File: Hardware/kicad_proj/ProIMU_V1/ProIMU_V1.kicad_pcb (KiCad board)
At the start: 2 copper layers, 50 x 50 mm, 31 parts, among them J1 USB4105-GF-A, J2 502570-0893, U1 BMP280, U2 MPU-9250, U3 STM32F412CEU6, U4 AIR602, U5 POGOPIN, U6 POGOPIN, U7 POGOPIN, U8 POGOPIN, U9 POGOPIN

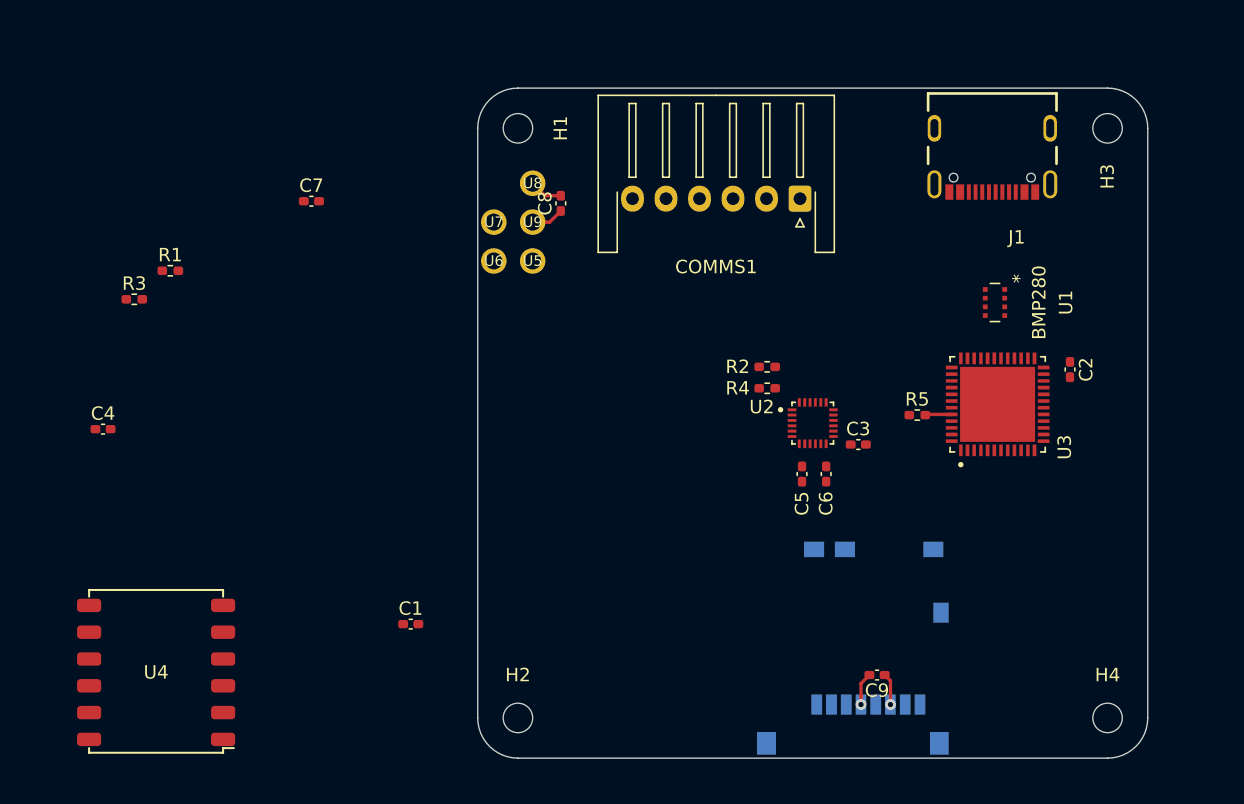
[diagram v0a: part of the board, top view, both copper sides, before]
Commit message: Update: Layout updated. Pinout needs to be revised
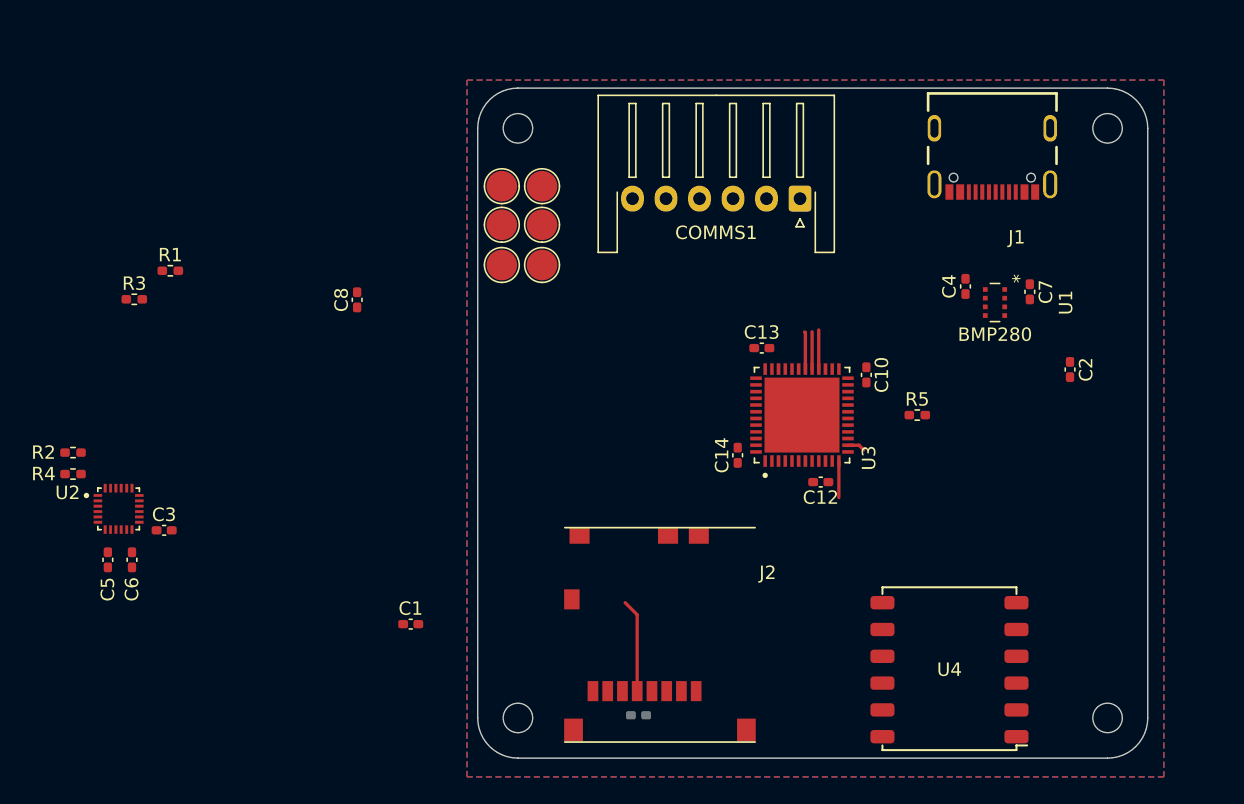
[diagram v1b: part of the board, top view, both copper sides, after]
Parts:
- added C10: 1uF, Capacitor_SMD:C_0402_1005Metric_Pad0.74x0.62mm_HandSolder, F.Cu at (155.8, 92.0)
- added C12: 1uF, Capacitor_SMD:C_0402_1005Metric_Pad0.74x0.62mm_HandSolder, F.Cu at (152.4, 100.0)
- added C13: 1uF, Capacitor_SMD:C_0402_1005Metric_Pad0.74x0.62mm_HandSolder, F.Cu at (148.0, 90.0)
- added C14: 1uF, Capacitor_SMD:C_0402_1005Metric_Pad0.74x0.62mm_HandSolder, F.Cu at (146.2, 98.0)
- added U10: POGOPIN, footprints:Test_Point, F.Cu at (131.6, 83.8)
- C9: moved to B.Cu
- J2: moved to F.Cu
- U5, U6, U7, U8, U9: footprint footprints:1.27MM_POGO -> footprints:Test_Point
- moved C4 65.2 mm to (163.2, 85.4), turned to -90 degrees
- moved U4 59.2 mm to (162.0, 114.0)
- moved C7 54.0 mm to (168.0, 85.8), turned to 90 degrees
- moved C6 52.2 mm to (101.0, 105.8)
- moved R2 52.2 mm to (96.6, 97.8)
- moved R4 52.2 mm to (96.6, 99.4)
- moved U2 52.2 mm to (100.0, 102.0)
- moved C3 52.2 mm to (103.4, 103.6)
- moved C5 52.2 mm to (99.2, 105.8)
- moved C9 18.1 mm to (138.8, 117.4), turned to 0 degrees
- moved C8 16.8 mm to (117.8, 86.4)
- moved U3 14.6 mm to (151.0, 95.0)
- moved J2 14.4 mm to (140.4, 111.4), turned to 180 degrees
- moved U6 6.64 mm to (131.6, 77.9)
- moved U8 3.86 mm to (128.6, 80.8), turned to 90 degrees
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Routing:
- net /SDCARD_CLK: track 0.00 -> 9.89 mm
- net GND: track 4.87 -> 0.00 mm, vias 1 -> 0
- net /SDCARD_D2: track 0.00 -> 2.79 mm
- net /SDCARD_D1: track 0.00 -> 2.78 mm
- net /WIFI_UART_TX: track 0.00 -> 2.72 mm
- net +3V3: track 2.46 -> 0.00 mm, vias 1 -> 0
- net +5V: track 2.44 -> 0.00 mm
- net Net-(R5-Pad2): track 1.99 -> 0.00 mm
- net /WIFI_RES: track 0.00 -> 1.31 mm
- added copper zone on F.Cu, net +3V3
- added copper zone on B.Cu, net GND

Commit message: Update: PCB Layout
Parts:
- J2, U2: moved to B.Cu
- moved BAT1 151.3 mm to (46.0, 62.0)
- moved C9 83.8 mm to (55.2, 111.8)
- moved C5 54.1 mm to (45.4, 100.2)
- moved C6 54.1 mm to (47.2, 100.2)
- moved R3 54.1 mm to (47.4, 80.8)
- moved C1 54.1 mm to (68.0, 105.0)
- moved C3 54.1 mm to (49.6, 98.0)
- moved C8 54.1 mm to (64.0, 80.8)
- moved R1 54.1 mm to (50.1, 78.6)
- moved R2 54.1 mm to (42.8, 92.2)
- moved R4 54.1 mm to (42.8, 93.8)
- moved J1 53.0 mm to (114.7, 57.6)
- moved J2 48.7 mm to (135.0, 63.0)
- moved COMMS1 40.9 mm to (110.0, 81.0), turned to -90 degrees
- moved U4 40.3 mm to (125.0, 98.0)
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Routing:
- added copper zone on F.Cu, net GND
- removed copper zone on F.Cu, net +3V3
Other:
- outline, holes or cut-outs redrawn

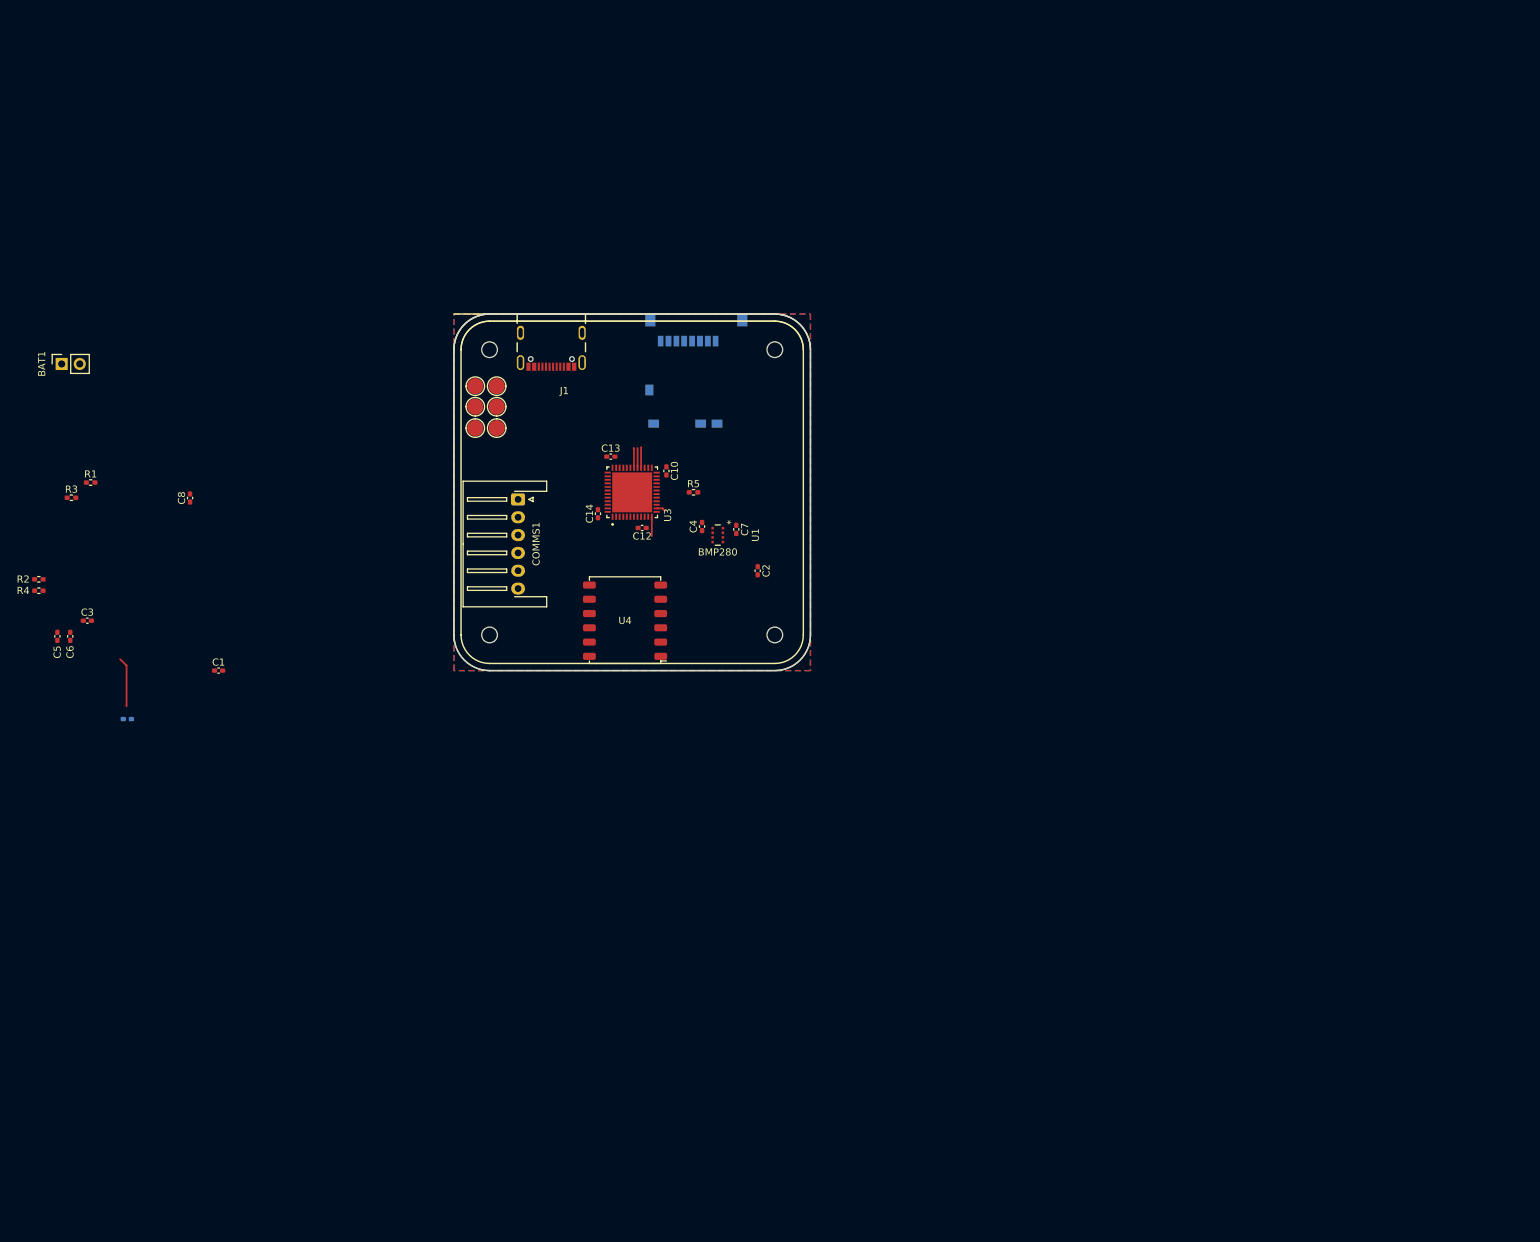
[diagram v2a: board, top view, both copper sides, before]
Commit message: Update: Layout Sorted. CAN Transreciever to be added and Debug pins to be updated
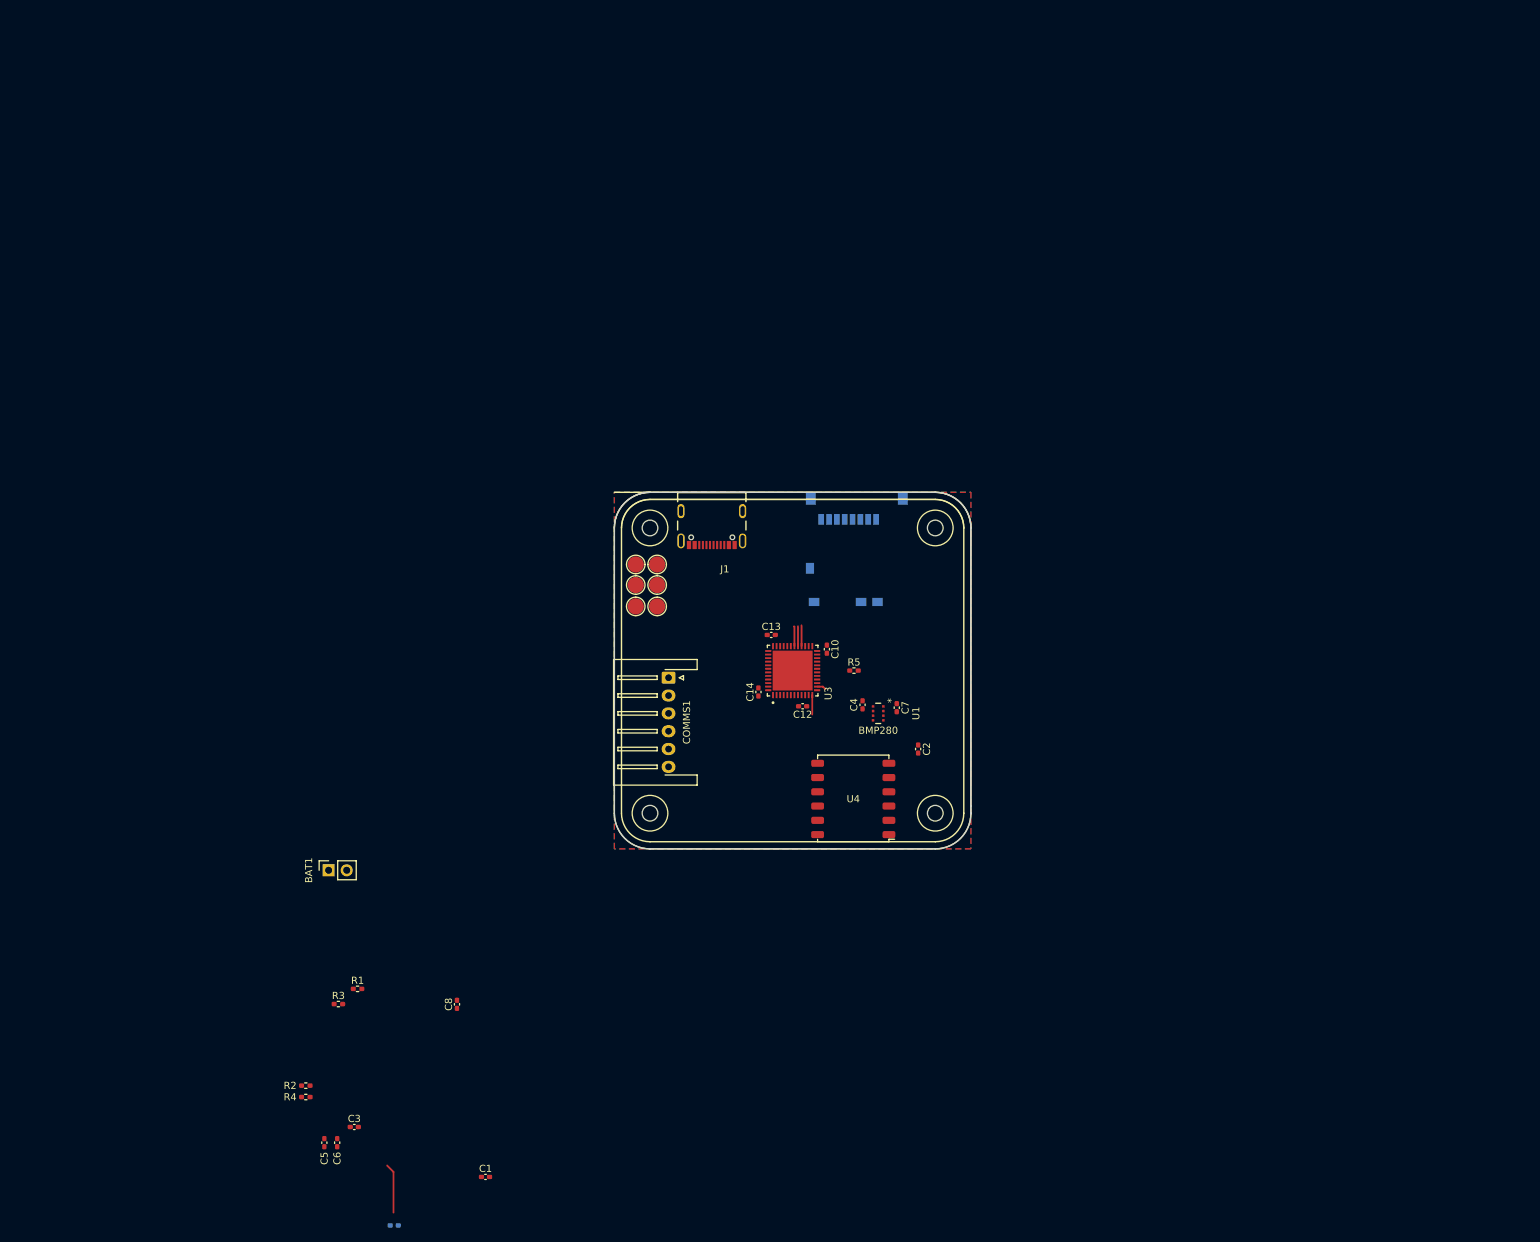
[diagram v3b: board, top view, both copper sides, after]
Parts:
- moved BAT1 80.3 mm to (83.4, 133.0)
- moved C1 80.3 mm to (105.4, 176.0)
- moved C3 80.3 mm to (87.0, 169.0)
- moved C5 80.3 mm to (82.8, 171.2)
- moved C8 80.3 mm to (101.4, 151.8)
- moved C9 80.3 mm to (92.6, 182.8)
- moved R1 80.3 mm to (87.5, 149.6)
- moved R4 80.3 mm to (80.2, 164.8)
- moved C6 80.3 mm to (84.6, 171.2)
- moved R2 80.3 mm to (80.2, 163.2)
- moved R3 80.3 mm to (84.8, 151.8)
- moved U4 40.6 mm to (157.0, 123.0)
- moved J1 33.6 mm to (137.2, 82.6)
- moved C10 33.6 mm to (153.3, 102.0)
- moved C12 33.6 mm to (149.9, 110.0)
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
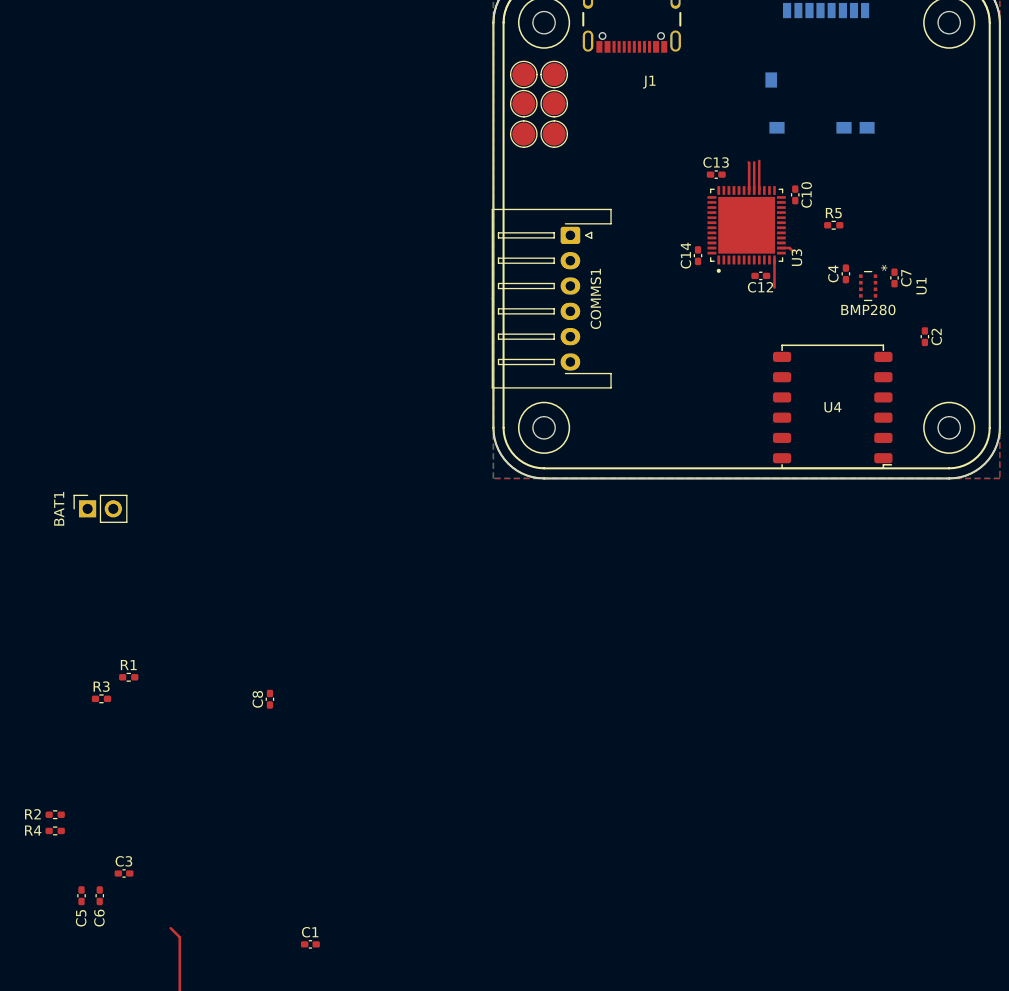
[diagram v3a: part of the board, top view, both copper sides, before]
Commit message: Update: Added CAN Transcreceiver
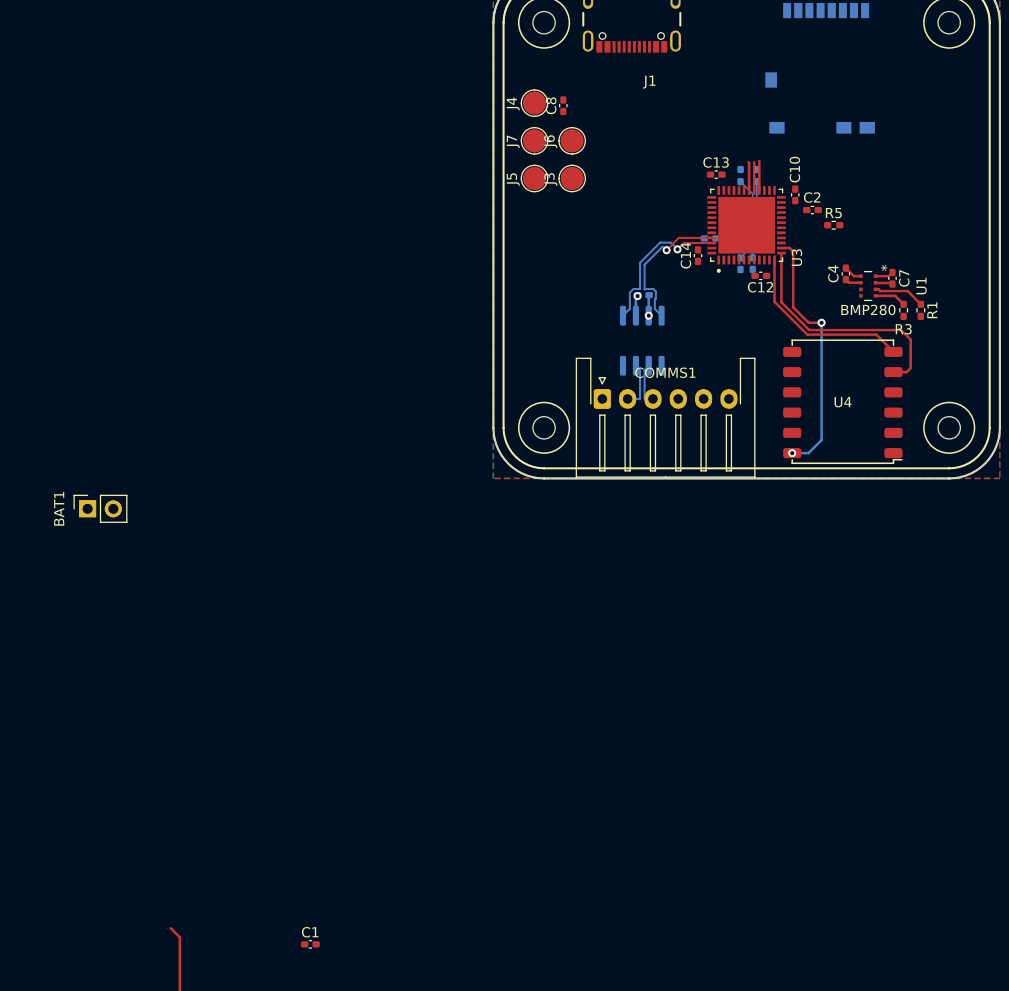
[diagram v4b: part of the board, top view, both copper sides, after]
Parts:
- removed U10, U5, U6, U7, U8, U9: POGOPIN, footprints:Test_Point
- added C11: 1uF, Capacitor_SMD:C_0402_1005Metric_Pad0.74x0.62mm_HandSolder, B.Cu at (138.3, 111.9)
- added J3: Conn_01x01, footprints:Test_Point, F.Cu at (131.3, 100.4)
- added J4: Conn_01x01, footprints:Test_Point, F.Cu at (127.6, 92.9)
- added J5: Conn_01x01, footprints:Test_Point, F.Cu at (127.6, 100.4)
- added J6: Conn_01x01, footprints:Test_Point, F.Cu at (131.3, 96.7)
- added J7: Conn_01x01, footprints:Test_Point, F.Cu at (127.6, 96.7)
- added U11: TJA1051T-3, Package_SO:SOIC-8_3.9x4.9mm_P1.27mm, B.Cu at (138.2, 116.4)
- C3, C5, C6, R2, R4: moved to B.Cu
- moved R4 94.8 mm to (149.5, 100.1), turned to 90 degrees
- moved R2 92.5 mm to (147.9, 100.1), turned to 90 degrees
- moved C5 91.0 mm to (149.1, 108.8)
- moved C6 88.9 mm to (147.9, 108.8)
- moved R3 88.0 mm to (164.0, 113.4), turned to -90 degrees
- moved R1 86.2 mm to (165.7, 113.4), turned to -90 degrees
- moved C3 85.3 mm to (144.9, 106.3), turned to 180 degrees
- moved C8 65.4 mm to (130.4, 93.2)
- moved C2 16.7 mm to (155.0, 103.5), turned to 180 degrees
- moved COMMS1 16.5 mm to (134.2, 122.2), turned to 0 degrees
- moved U4 1.12 mm to (158.0, 122.5)
- moved C7 0.20 mm to (162.9, 110.2)
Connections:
- COMMS1 pad 2: /CAN_TRX- -> /CAN+
- COMMS1 pad 3: /CAN_TRX+ -> /CAN-
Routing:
- net /WIFI_RES: track 1.31 -> 25.3 mm, vias 0 -> 2
- net /WIFI_UART_RX: track 0.00 -> 23.8 mm
- net /WIFI_UART_TX: track 2.72 -> 17.9 mm
- net /CAN_TRX+: track 0.00 -> 14.7 mm, vias 0 -> 1
- net /CAN_TRX-: track 0.00 -> 14.4 mm, vias 0 -> 1
- net GND: track 0.00 -> 5.61 mm, vias 0 -> 1
- net +5V: track 0.00 -> 5.45 mm, vias 0 -> 1
- net /BMP280_SCL: track 0.00 -> 5.09 mm
- net /CAN+: track 0.00 -> 4.64 mm
- net /CAN-: track 0.00 -> 4.24 mm
- net +3V3: track 0.00 -> 3.42 mm
- net /MPU9250_SCK: track 0.00 -> 3.25 mm
- net /BMP280_SDA: track 0.00 -> 3.12 mm
- net /MPU9250_SDA: track 0.00 -> 2.76 mm
- net Net-(C6-Pad1): track 0.00 -> 1.85 mm
